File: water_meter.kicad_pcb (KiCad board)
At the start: 4 copper layers, 94 x 64 mm, 50 parts, among them J1 2464, J2 Conn_01x02_Male, J3 Conn_01x06_Male, J4 USB_Micro-10118193-0001LF, J5 Conn_01x02_Male, J8 Conn_01x02_Male, U1 RT9080-33GJ5, U2 ESP32-S3-WROOM-1, U3 ALT025-10E, U4 SLG46826G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

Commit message: V2
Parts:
- removed CLK1, INT1, PIN4, PIN5, SCL1, SDA1, VBAT1: TestPoint, TestPoint:TestPoint_Pad_D2.0mm
- removed D1: WS2812B, LED_SMD:LED_WS2812B_PLCC4_5.0x5.0mm_P3.2mm
- removed J2: Conn_01x02_Male, Connector_PinSocket_2.54mm:PinSocket_1x02_P2.54mm_Vertical
- added C16: 0.1uF, Capacitor_SMD:C_0805_2012Metric, F.Cu at (175.2, 109.0)
- added Q1: BSS84, Package_TO_SOT_SMD:SOT-23, F.Cu at (175.2, 132.3)
- added Q2: BSS84, Package_TO_SOT_SMD:SOT-23, F.Cu at (144.0, 114.0)
- added R10: 100k, Resistor_SMD:R_0805_2012Metric, F.Cu at (176.1, 137.2)
- added R11: 500R, Resistor_SMD:R_0805_2012Metric, F.Cu at (150.1, 111.3)
- added R12: 500R, Resistor_SMD:R_0805_2012Metric, F.Cu at (139.2, 109.5)
- added R13: 500R, Resistor_SMD:R_0805_2012Metric, F.Cu at (139.2, 113.0)
- added R8: 100k, Resistor_SMD:R_0805_2012Metric, F.Cu at (179.7, 102.2)
- added U6: IN-PI22TAT5R5G5B, Nabil:INPI22TAT5R5G5B, F.Cu at (157.3, 116.8)
- added U7: 10413_lens, Nabil:10414_Lens, F.Cu at (157.3, 116.8)
- added U8: FM24C64C, Package_SO:SOIC-8_3.9x4.9mm_P1.27mm, F.Cu at (131.0, 98.5)
- C1, C10, C11, C12, C13, C14, C15, C2, C3, C4, C6, C7, C8, C9: footprint Capacitor_SMD:C_0805_2012Metric_Pad1.18x1.45mm_HandSolder -> Capacitor_SMD:C_0805_2012Metric
- C5: value 10uF/25V(20%) -> 10uF; footprint Capacitor_SMD:C_0805_2012Metric_Pad1.18x1.45mm_HandSolder -> Capacitor_SMD:C_0805_2012Metric
- D2: footprint LED_SMD:LED_0805_2012Metric_Pad1.15x1.40mm_HandSolder -> LED_SMD:LED_0805_2012Metric
- F1: footprint Fuse:Fuse_1206_3216Metric_Pad1.42x1.75mm_HandSolder -> Fuse:Fuse_1206_3216Metric
- H1, H2, H3, H4: footprint MountingHole:MountingHole_2.5mm -> MountingHole:MountingHole_2.5mm_Pad
- R1: value 10k(1%) -> 10k; footprint Resistor_SMD:R_0805_2012Metric_Pad1.20x1.40mm_HandSolder -> Resistor_SMD:R_0805_2012Metric
- R2, R3, R4, R5, R6, R7, R9: footprint Resistor_SMD:R_0805_2012Metric_Pad1.20x1.40mm_HandSolder -> Resistor_SMD:R_0805_2012Metric
- U2: footprint Espressif:ESP32-S3-WROOM-1 -> Espressif:ESP32-S3-WROOM-1U
- Y1: value 32.768kHz (ESR < 70 kΩ) -> ABS07-32.768KHZ-T; footprint Crystal:Crystal_SMD_G8-2Pin_3.2x1.5mm_HandSoldering -> Nabil:XTAL_ABS07-32.768KHZ-T
- Y2: value Crystal -> ABS07-32.768KHZ-T; footprint Crystal:Crystal_C38-LF_D3.0mm_L8.0mm_Vertical -> Nabil:XTAL_ABS07-32.768KHZ-T
- moved C15 50.3 mm to (150.1, 115.6), turned to 90 degrees
- moved R1 48.3 mm to (122.2, 138.8)
- moved C3 47.9 mm to (122.2, 141.8)
- moved C8 36.9 mm to (173.4, 102.2), turned to -90 degrees
- moved C14 36.9 mm to (176.6, 102.2), turned to -90 degrees
- moved R7 35.0 mm to (198.8, 120.6), turned to 0 degrees
- moved U5 30.8 mm to (185.3, 101.4)
- moved C13 30.6 mm to (192.8, 99.6)
- moved C7 30.3 mm to (192.8, 104.3), turned to 90 degrees
- moved C12 25.3 mm to (162.3, 100.4), turned to 45 degrees
- moved J5 25.3 mm to (171.2, 110.1)
- moved Y2 25.1 mm to (196.9, 102.1)
- moved J3 24.7 mm to (117.1, 121.9)
- moved U3 24.6 mm to (157.3, 98.2)
- moved U4 23.9 mm to (171.6, 118.2)
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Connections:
- C15 pad 1: /LED_PIN0 -> Net-(Q2-Pad3)
- J1 pad 1: Net-(J2-Pad2) -> /VBATT
- J5 pad 2: +3V3 -> /SLG_PWR
- U2 pad 39: unconnected-(U2-Pad39) -> /LED_PWR
- U2 pad 6: unconnected-(U2-Pad6) -> /RTC_INT
- U2 pad 7: unconnected-(U2-Pad7) -> /SLG_PWR_GPIO
- U3 pad 6: +3V3 -> /MAG_PWR
- U4 pad 20: +3V3 -> /SLG_PWR
- U4 pad 4: Net-(U4-Pad4) -> unconnected-(U4-Pad4)
- U4 pad 5: Net-(U4-Pad5) -> /MAG_PWR
- U4 pad 8: unconnected-(U4-Pad8) -> /SLG_INT2
- U4 pad 9: /SLG_INT2 -> unconnected-(U4-Pad9)
- U5 pad 3: Net-(U5-Pad3) -> /RTC_INT
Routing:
- net +3V3: track 97.8 -> 341.0 mm, vias 8 -> 14
- net /SDA: track 71.8 -> 175.9 mm, vias 0 -> 4
- net /RTC_INT: track 0.00 -> 92.0 mm, vias 0 -> 4
- net /SCL: track 75.6 -> 156.3 mm, vias 0 -> 4
- net /LED_PIN0: track 8.82 -> 59.4 mm, vias 0 -> 2
- net /SLG_PWR: track 0.00 -> 39.9 mm
- net /LED_PWR: track 0.00 -> 36.3 mm, vias 0 -> 2
- net /SLG_PWR_GPIO: track 0.00 -> 36.1 mm
- net /MAG_PWR: track 0.00 -> 33.7 mm, vias 0 -> 2
- net GND: track 17.7 -> 42.6 mm, vias 0 -> 39
- net Net-(U4-Pad4): track 23.1 -> 0.00 mm
- net Net-(U4-Pad5): track 20.9 -> 0.00 mm
- net /EN: track 17.8 -> 37.8 mm, vias 0 -> 1
- net Net-(Q2-Pad3): track 0.00 -> 13.2 mm
- net /M_CLK: track 17.3 -> 30.1 mm, vias 0 -> 2
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- added copper zone on B.Cu, net GND
- removed copper zone on B.Cu, net +3V3
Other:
- board text added: "3V3"
- board text added: "SCL"
- board text added: "SDA"
- board text removed: "3V"
- board text removed: "Keepout?"

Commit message: V3
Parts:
- removed J8: Conn_01x02_Male, Connector_PinSocket_2.54mm:PinSocket_1x02_P2.54mm_Vertical
- removed Q1: BSS84, Package_TO_SOT_SMD:SOT-23
- removed U7: 10413_lens, Nabil:10414_Lens
- added C17: 0.1uF, Capacitor_SMD:C_0805_2012Metric, F.Cu at (121.3, 96.4)
- added C18: 0.1uF, Capacitor_SMD:C_0805_2012Metric, F.Cu at (159.4, 111.2)
- added C19: 0.1uF, Capacitor_SMD:C_0805_2012Metric, F.Cu at (178.6, 127.6)
- added J2: Conn_01x02_Male, Jumper:SolderJumper-2_P1.3mm_Bridged_Pad1.0x1.5mm, F.Cu at (155.8, 122.4)
- added J6: Conn_01x08_Female, Connector_JST:JST_SH_SM08B-SRSS-TB_1x08-1MP_P1.00mm_Horizontal, B.Cu at (201.0, 128.5)
- added J7: Conn_01x04_Female, Connector_JST:JST_SH_SM04B-SRSS-TB_1x04-1MP_P1.00mm_Horizontal, B.Cu at (201.0, 106.5)
- added Q3: BSS84, Package_TO_SOT_SMD:SOT-23, F.Cu at (185.1, 123.8)
- added R14: 10M, Resistor_SMD:R_0805_2012Metric, F.Cu at (178.6, 134.6)
- added R15: 100k, Resistor_SMD:R_0805_2012Metric, F.Cu at (150.8, 110.4)
- added R16: 50k, Resistor_SMD:R_0805_2012Metric, F.Cu at (164.3, 105.0)
- added R17: 50k, Resistor_SMD:R_0805_2012Metric, F.Cu at (161.8, 104.9)
- added R18: 1M, Resistor_SMD:R_0805_2012Metric, F.Cu at (166.4, 115.4)
- added R19: 1M, Resistor_SMD:R_0805_2012Metric, F.Cu at (167.1, 124.0)
- added S1: PTS526_SK15_SMTR2_LFS, Nabil:PTS526SK15SMTR2LFS, F.Cu at (115.0, 96.8)
- added TP1: TestPoint, TestPoint:TestPoint_Pad_D1.0mm, F.Cu at (168.6, 113.1)
- added U9: SLG88103V, Nabil:SLG88103V, F.Cu at (172.9, 116.9)
- C16: value 0.1uF -> 100pF
- H1, H2, H3, H4: value MountingHole_Pad -> MountingHole; footprint MountingHole:MountingHole_2.5mm_Pad -> MountingHole:MountingHole_6mm
- J3, U6: moved to B.Cu
- J5: value Conn_01x02_Male -> Conn_01x04_Male; footprint Jumper:SolderJumper-2_P1.3mm_Bridged_Pad1.0x1.5mm -> Connector_PinHeader_2.54mm:PinHeader_1x04_P2.54mm_Vertical; moved to B.Cu
- R10: value 100k -> 10M
- R11: value 500R -> 2k
- R12: value 500R -> 1k
- R6: value 5.1K -> 4.7k
- U4: value SLG46826G -> SLG47004V; footprint Nabil:SOP65P640X120-20N -> Nabil:STQFN-24-3.0X3.0-A
- U8: value FM24C64C -> MB85RC64TA
- moved U6 48.0 mm to (114.8, 94.7), turned to 180 degrees
- moved C16 27.1 mm to (148.2, 110.5)
- moved C15 24.6 mm to (133.1, 97.8), turned to -90 degrees
- moved J5 23.1 mm to (193.6, 115.5), turned to 180 degrees
- moved Q2 21.8 mm to (129.4, 97.8), turned to 90 degrees
- moved R8 20.3 mm to (199.9, 99.7), turned to 90 degrees
- moved C14 19.9 mm to (195.5, 95.9)
- moved C8 19.9 mm to (192.2, 95.9)
- moved R11 19.6 mm to (135.8, 97.8), turned to -90 degrees
- moved U8 17.7 mm to (136.5, 115.3), turned to 0 degrees
- moved R13 15.0 mm to (128.5, 102.5), turned to 90 degrees
- moved U4 14.7 mm to (156.9, 116.8), turned to 90 degrees
- moved Y2 14.5 mm to (182.6, 100.3), turned to 90 degrees
- moved C11 13.8 mm to (165.3, 100.0), turned to 0 degrees
- moved R7 11.3 mm to (188.8, 115.4), turned to 180 degrees
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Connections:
- C11 pad 1: /MAG- -> /Sensors/MAG-
- C12 pad 1: /MAG+ -> /Sensors/MAG+
- C16 pad 1: GND -> /MAG
- C16 pad 2: /SLG_PWR -> GND
- J1 pad 1: /VBATT -> Net-(J1-Pad1)
- J5 pad 1: Net-(J5-Pad1) -> +3V3
- J5 pad 2: /SLG_PWR -> /SCL
- R10 pad 1: GND -> /VBATT
- R10 pad 2: /SLG_PWR_GPIO -> /VBATT_DIV
- U2 pad 6: /RTC_INT -> /VBATT_DIV
- U2 pad 7: /SLG_PWR_GPIO -> /MAG
- U3 pad 1: /MAG+ -> /Sensors/MAG+
- U3 pad 4: /MAG- -> /Sensors/MAG-
- U3 pad 6: /MAG_PWR -> /Sensors/MAG_PWR
- U4 pad 1: /MAG+ -> Net-(J2-Pad1)
- U4 pad 10: GND -> /SCL
- U4 pad 11: unconnected-(U4-Pad11) -> /SDA
- U4 pad 12: /SDA -> /Sensors/MAG_PWR
- U4 pad 13: /SCL -> +3V3
- U4 pad 14: unconnected-(U4-Pad14) -> GND
- U4 pad 15: unconnected-(U4-Pad15) -> Net-(R15-Pad1)
- U4 pad 16: unconnected-(U4-Pad16) -> /MAG
- U4 pad 17: unconnected-(U4-Pad17) -> /VBATT_DIV
- U4 pad 18: unconnected-(U4-Pad18) -> /SLG_INT1
- U4 pad 19: /M_CLK -> /SLG_PIN19
- U4 pad 2: /MAG- -> GND
- U4 pad 20: /SLG_PWR -> /SLG_INT2
- U4 pad 3: /VBATT -> unconnected-(U4-Pad3)
- U4 pad 5: /MAG_PWR -> unconnected-(U4-Pad5)
- U4 pad 6: /SLG_INT1 -> /Sensors/RH0_A
- U4 pad 7: Net-(J5-Pad1) -> /Sensors/RH0_B
- U4 pad 8: /SLG_INT2 -> /Sensors/RH1_A
- U4 pad 9: unconnected-(U4-Pad9) -> /Sensors/RH1_B
- U5 pad 3: /RTC_INT -> unconnected-(U5-Pad3)
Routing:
- net +3V3: track 341.0 -> 14.0 mm, vias 14 -> 32
- net /MAG: track 0.00 -> 154.2 mm, vias 0 -> 4
- net /VBATT_DIV: track 0.00 -> 119.8 mm, vias 0 -> 5
- net GND: track 42.6 -> 149.9 mm
- net /M_CLK: track 30.1 -> 128.1 mm, vias 2 -> 3
- net /RTC_INT: track 92.0 -> 0.00 mm, vias 4 -> 0
- net /SLG_INT2: track 25.9 -> 112.4 mm, vias 0 -> 1
- net /SLG_INT1: track 25.9 -> 112.3 mm, vias 0 -> 1
- net /SLG_PIN19: track 0.00 -> 56.1 mm, vias 0 -> 1
- net /EN: track 37.8 -> 88.2 mm, vias 1 -> 2
- net /SLG_PWR: track 39.9 -> 0.00 mm
- net /SLG_PWR_GPIO: track 36.1 -> 0.00 mm
- net /VBATT: track 49.9 -> 15.8 mm, vias 4 -> 0
- net /MAG_PWR: track 33.7 -> 0.00 mm, vias 2 -> 0
- net /MAG-: track 32.1 -> 0.00 mm
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- added copper zone on B.Cu, net +3V3
- added copper zone on F.Cu, net +3V3
- added copper zone on In1.Cu, net GND
- added copper zone on In2.Cu, net GND
- removed copper zone on B.Cu, net GND
- removed copper zone on F.Cu, net GND
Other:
- board text added: "WayWayWay"

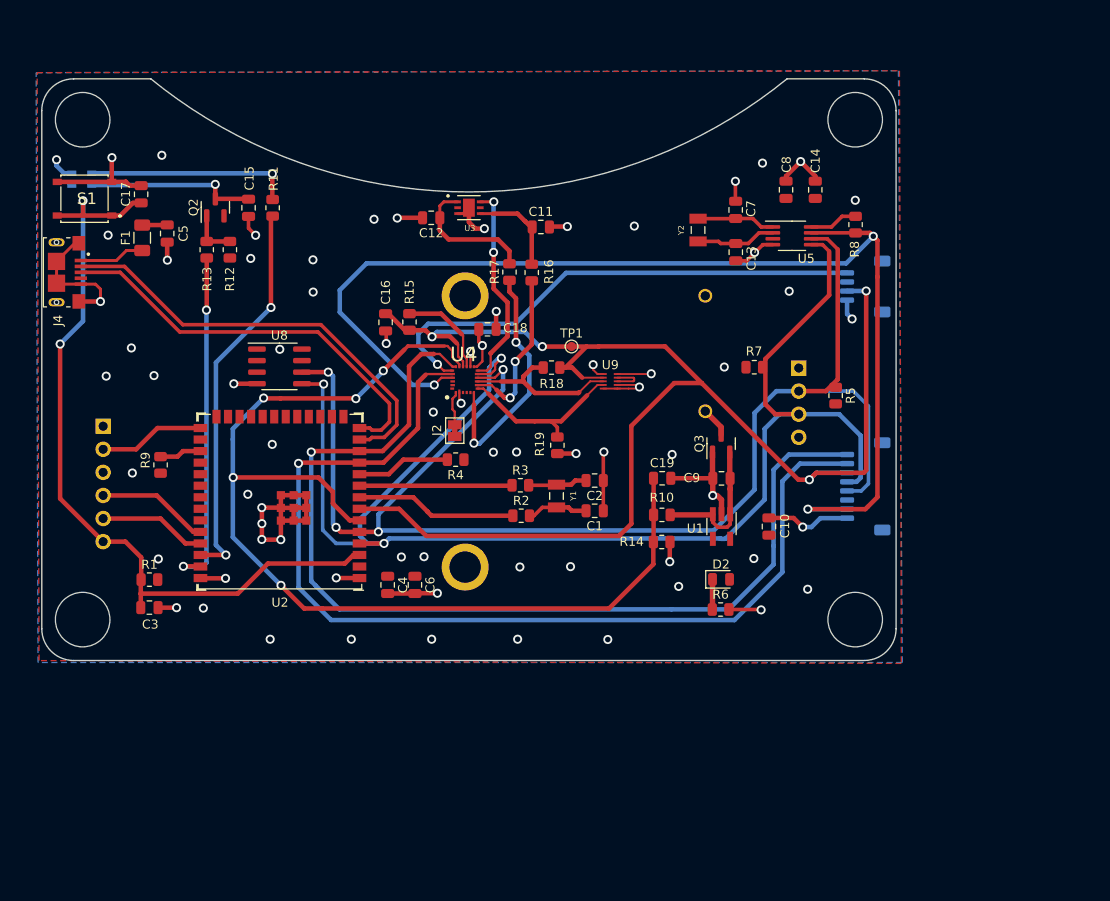
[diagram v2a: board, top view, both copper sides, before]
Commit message: Prototype V0.4   - New board layout for new enclosure   - Added user button   - Using opamp power down pin to save power
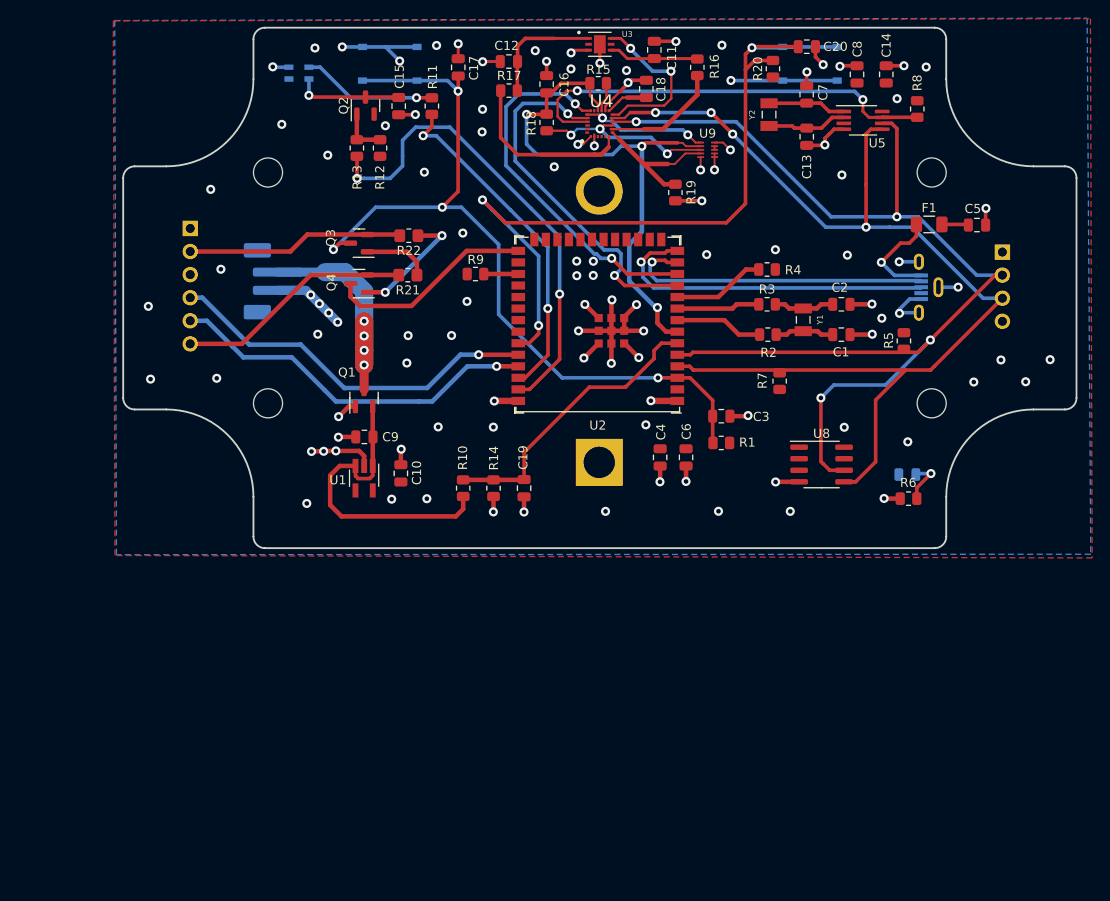
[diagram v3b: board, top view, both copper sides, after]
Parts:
- removed J2: Conn_01x02_Male, Jumper:SolderJumper-2_P1.3mm_Bridged_Pad1.0x1.5mm
- removed J7: Conn_01x04_Female, Connector_JST:JST_SH_SM04B-SRSS-TB_1x04-1MP_P1.00mm_Horizontal
- removed TP1: TestPoint, TestPoint:TestPoint_Pad_D1.0mm
- added C20: 0.1uF, Capacitor_SMD:C_0805_2012Metric, F.Cu at (194.5, 80.1)
- added Q1: BSS84, Package_TO_SOT_SMD:SOT-23, F.Cu at (145.8, 118.8)
- added Q4: MMBT3904, Package_TO_SOT_SMD:SOT-23, F.Cu at (145.2, 106.2)
- added R20: 10k, Resistor_SMD:R_0805_2012Metric, F.Cu at (190.8, 82.5)
- added R21: 10K, Resistor_SMD:R_0805_2012Metric_Pad1.20x1.40mm_HandSolder, F.Cu at (150.6, 105.3)
- added R22: 10K, Resistor_SMD:R_0805_2012Metric_Pad1.20x1.40mm_HandSolder, F.Cu at (150.7, 100.9)
- added S2: PTS526_SK15_SMTR2_LFS, Nabil:PTS526SK15SMTR2LFS, B.Cu at (194.9, 82.0)
- D2, S1: moved to B.Cu
- H1, H2, H3, H4: footprint MountingHole:MountingHole_6mm -> MountingHole:MountingHole_3.2mm_M3
- J1: value 2464 -> Conn_01x02_Female; footprint Nabil:2464 -> Nabil:JST_PH_B2B-PH-SM4-TB_1x02-1MP_P2.00mm_Vertical
- J4: value USB_Micro-10118193-0001LF -> USB_B_Micro; footprint Nabil:FCI_10118193-0001LF -> Nabil:USB_Micro-B_Molex-105133-0001; moved to B.Cu
- J6: value Conn_01x08_Female -> 2465; footprint Connector_JST:JST_SH_SM08B-SRSS-TB_1x08-1MP_P1.00mm_Horizontal -> Nabil:2465
- Q3: value BSS84 -> MMBT3904
- R12: value 1k -> 10k
- U3: value ALT025-10E -> ALT021-10E
- moved H1 98.5 mm to (208.3, 119.4)
- moved J4 96.0 mm to (207.9, 106.6)
- moved C5 89.1 mm to (213.2, 99.8), turned to 180 degrees
- moved F1 86.6 mm to (208.0, 99.7), turned to 180 degrees
- moved C3 66.4 mm to (185.1, 120.8)
- moved H3 64.9 mm to (135.2, 94.0)
- moved R1 64.7 mm to (185.1, 123.7)
- moved U8 60.6 mm to (196.2, 126.1)
- moved H4 49.9 mm to (208.3, 94.0)
- moved Q3 45.5 mm to (145.2, 101.7), turned to 180 degrees
- moved C10 40.9 mm to (149.9, 127.1)
- moved R9 40.5 mm to (158.1, 105.1), turned to 0 degrees
- moved R4 40.1 mm to (190.2, 104.6)
- moved U2 40.0 mm to (171.5, 110.8)
- moved U1 39.7 mm to (145.8, 127.6)
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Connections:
- J3 pad 2: /GPIO0 -> /RTS
- J3 pad 6: /EN -> /DTR
- Q3 pad 1: GND -> Net-(Q3-Pad1)
- Q3 pad 2: /VBATT -> /RTS
- Q3 pad 3: Net-(J1-Pad1) -> /EN
- U2 pad 35: unconnected-(U2-Pad35) -> /USER_INPUT
- U4 pad 1: Net-(J2-Pad1) -> +3V3
- U4 pad 17: /VBATT_DIV -> unconnected-(U4-Pad17)
- U4 pad 19: /SLG_PIN19 -> /Sensors/OP_AMP_PWR_DOWN
- U9 pad 1: GND -> /Sensors/OP_AMP_PWR_DOWN
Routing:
- net /MAG: track 154.2 -> 60.7 mm, vias 4 -> 3
- net /VBATT_DIV: track 119.8 -> 32.0 mm, vias 5 -> 0
- net /USER_INPUT: track 0.00 -> 86.3 mm, vias 0 -> 3
- net /M_CLK: track 128.1 -> 47.3 mm, vias 3 -> 2
- net /SLG_INT2: track 112.4 -> 40.4 mm, vias 1 -> 2
- net /SLG_INT1: track 112.3 -> 41.0 mm, vias 1 -> 2
- net /SLG_PIN19: track 56.1 -> 0.00 mm, vias 1 -> 0
- net /SDA: track 157.8 -> 119.0 mm, vias 3 -> 4
- net /UART0_TX: track 11.8 -> 41.4 mm, vias 0 -> 1
- net /UART0_RX: track 12.4 -> 41.7 mm, vias 0 -> 1
- net /SCL: track 151.7 -> 125.5 mm
- net /DTR: track 0.00 -> 26.1 mm
- net /RTS: track 0.00 -> 23.9 mm
- net Net-(J1-Pad1): track 3.36 -> 26.0 mm, vias 0 -> 4
- net /VBATT: track 15.8 -> 34.2 mm
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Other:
- board size 94 x 64 mm -> 104.9 x 57.3 mm
- board text added: "Reset"
- board text added: "User"
- board text added: "YDrip: V0.4"
- board text removed: "WayWayWay"
